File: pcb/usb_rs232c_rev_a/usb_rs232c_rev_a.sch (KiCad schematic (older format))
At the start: 29 parts, among them J1 USB_A, J2 RS-232, U1 CH340G, U2 MAX232, Y1 12MHz

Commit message: Updated PCB after the first iteration.
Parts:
- MH1, MH2: value 1.3mm -> 1.4mm; footprint usb_rs232_footprints:MountingHole_1.3mm -> usb_rs232_footprints:MountingHole_1.4mm
- TP1, TP2: footprint Measurement_Points:Measurement_Point_Round-SMD-Pad_Small -> usb_rs232_footprints:Measurement_Point_Square-SMD_1.0mmx1.0mm
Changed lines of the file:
@@
 F 0 "TP1" H 2600 1400 50  0000 C BNN
 F 1 "5V" H 2600 1350 50  0000 C CNN
-F 2 "Measurement_Points:Measurement_Point_Round-SMD-Pad_Small" H 2600 1100 50  0001 C CNN
+F 2 "usb_rs232_footprints:Measurement_Point_Square-SMD_1.0mmx1.0mm" H 2600 1100 50  0001 C CNN
 F 3 "" H 2600 1100 50  0001 C CNN
 	1    2600 1100
@@
 F 0 "TP2" H 2600 4700 50  0000 C BNN
 F 1 "GND" H 2600 4650 50  0000 C CNN
-F 2 "Measurement_Points:Measurement_Point_Round-SMD-Pad_Small" H 2600 4400 50  0001 C CNN
+F 2 "usb_rs232_footprints:Measurement_Point_Square-SMD_1.0mmx1.0mm" H 2600 4400 50  0001 C CNN
 F 3 "" H 2600 4400 50  0001 C CNN
 	1    2600 4400
@@
 P 5800 4100
 F 0 "MH1" H 5800 4200 50  0000 C CNN
-F 1 "1.3mm" H 5800 4000 50  0000 C CNN
-F 2 "usb_rs232_footprints:MountingHole_1.3mm" H 5800 4100 50  0001 C CNN
+F 1 "1.4mm" H 5800 4000 50  0000 C CNN
+F 2 "usb_rs232_footprints:MountingHole_1.4mm" H 5800 4100 50  0001 C CNN
 F 3 "" H 5800 4100 50  0001 C CNN
 	1    5800 4100
@@
 P 6100 4100
 F 0 "MH2" H 6100 4200 50  0000 C CNN
-F 1 "1.3mm" H 6100 4000 50  0000 C CNN
-F 2 "usb_rs232_footprints:MountingHole_1.3mm" H 6100 4100 50  0001 C CNN
+F 1 "1.4mm" H 6100 4000 50  0000 C CNN
+F 2 "usb_rs232_footprints:MountingHole_1.4mm" H 6100 4100 50  0001 C CNN
 F 3 "" H 6100 4100 50  0001 C CNN
 	1    6100 4100

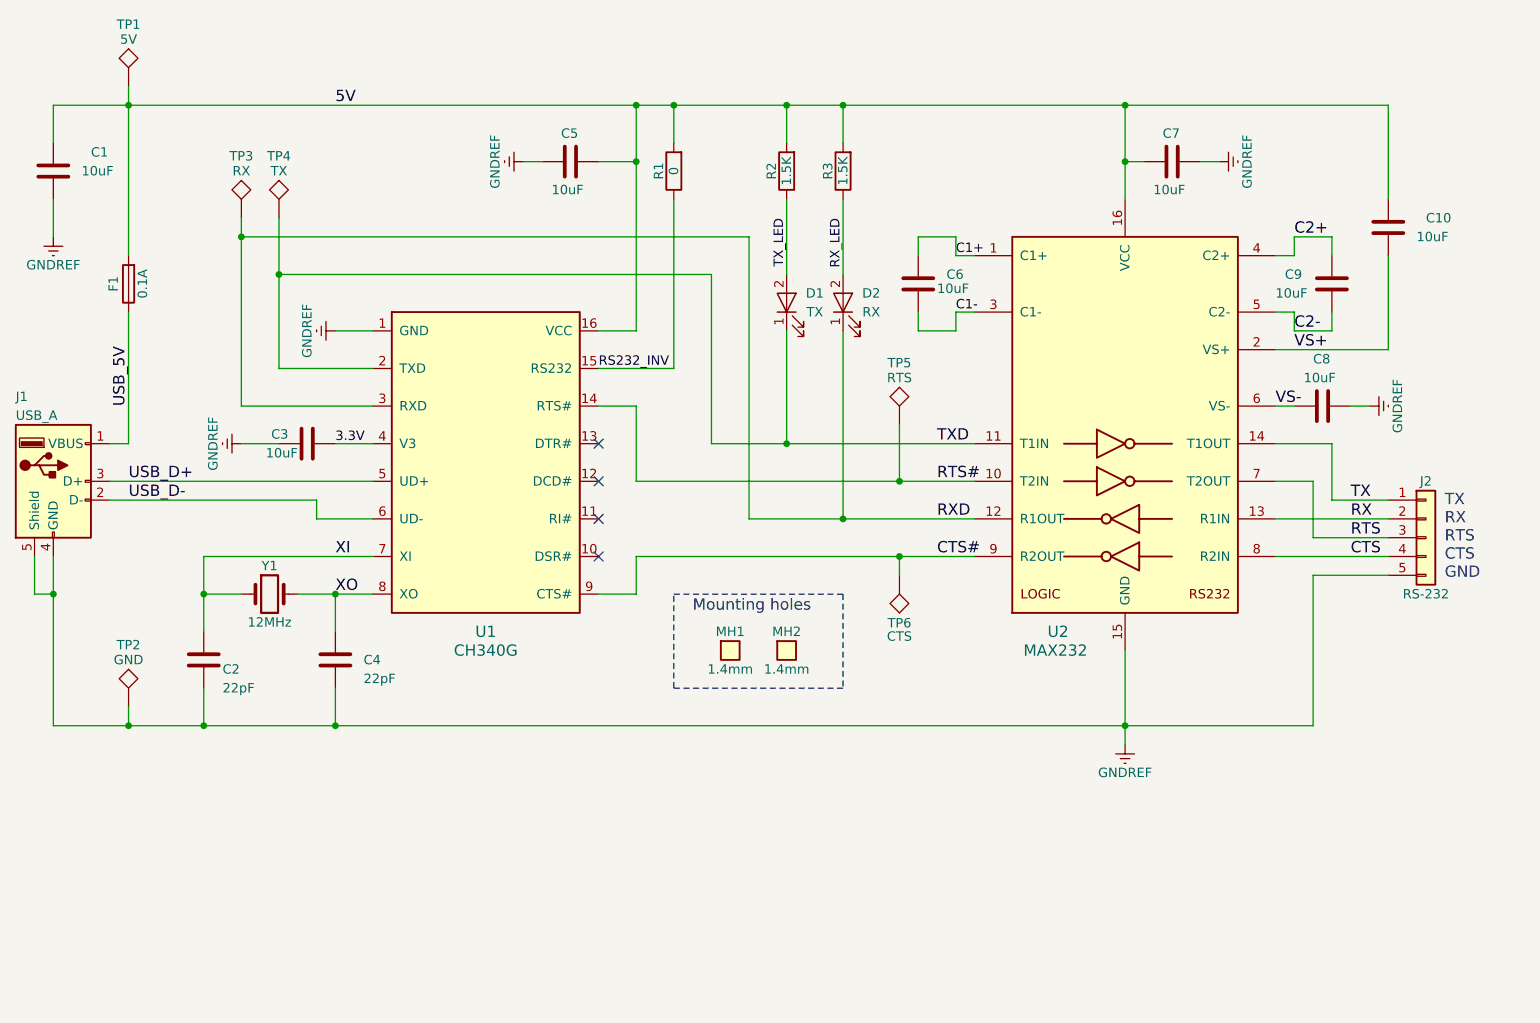
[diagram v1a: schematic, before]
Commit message: 1. Added bypass resistors for MAX232. 2. Updated README.md
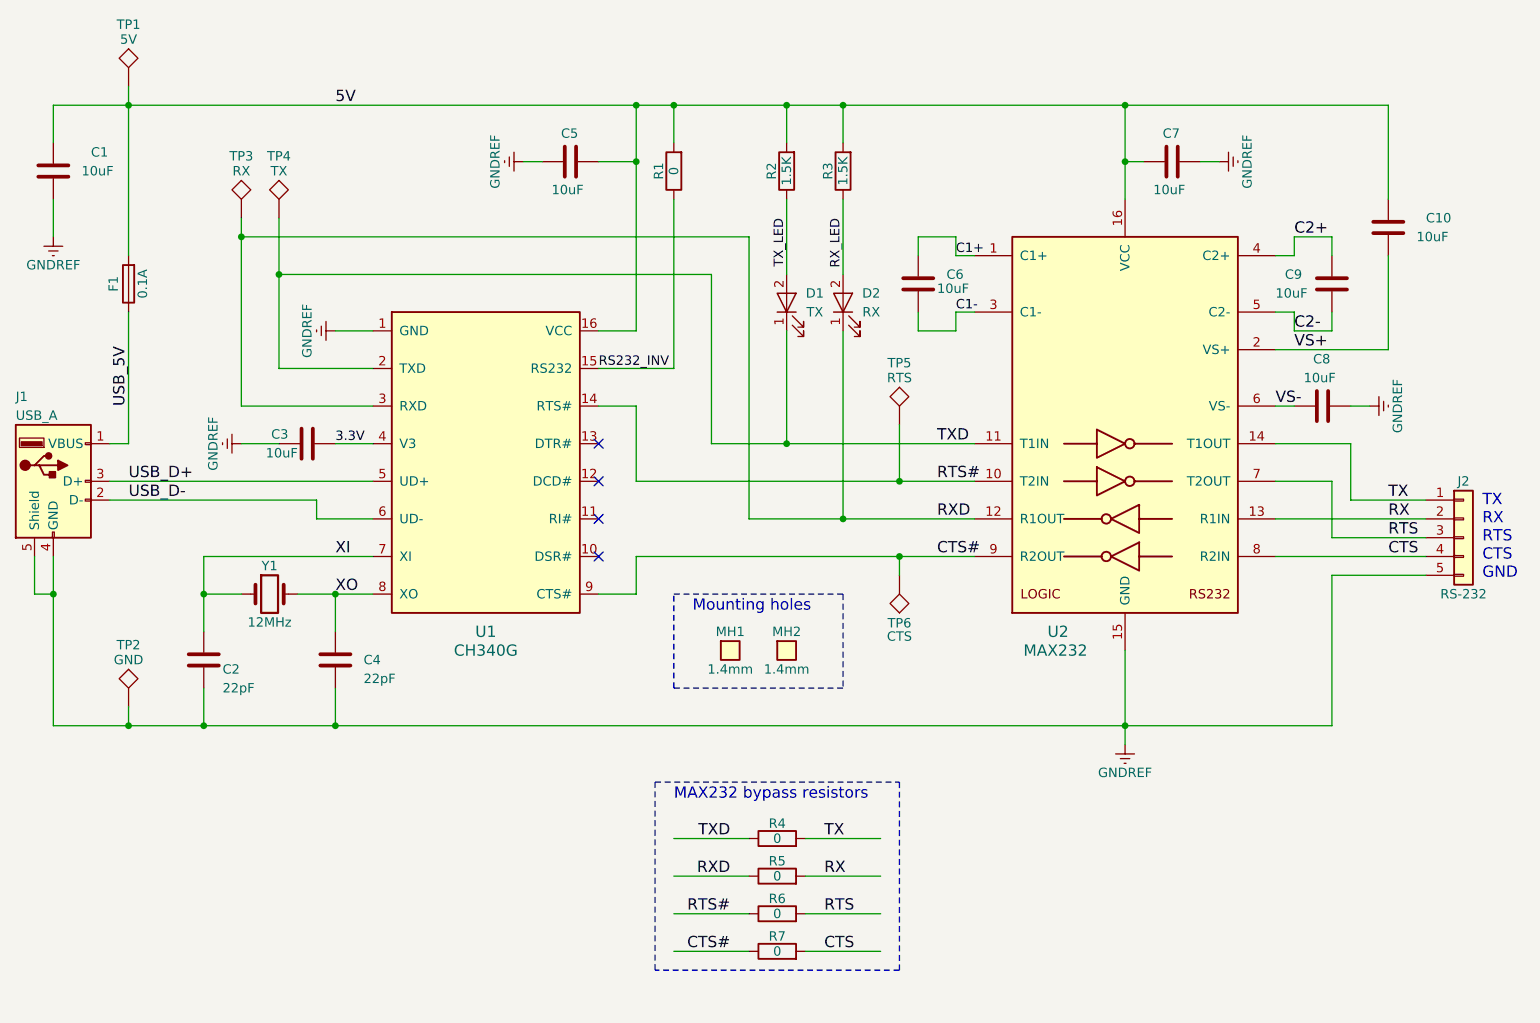
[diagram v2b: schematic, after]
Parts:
- added R4, R5, R6, R7: 0, Resistors_SMD:R_0603, symbol R
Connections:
- wire segments 91 -> 122
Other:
- note added: "MAX232 bypass resistors"
- moved on the sheet: J2

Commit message: Schematics update.
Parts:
- C10, C6, C8, C9: value 10uF -> 1uF
- C3: value 10uF -> 10nF
- C5: value 10uF -> 100nF
- J2: value RS-232 -> RS-232/UART
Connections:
- wire segments 122 -> 99
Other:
- note added: "BYPASS RESISTORS\n------------\n\nBypass resistors are assembled if RS-232 is not required.\nNormally 0 Ohm resistors may be used.\nTheir values may be increased up to hundreds of Ohms\nif current limiting is desired."
- moved on the sheet: R4, R5, R6, R7
